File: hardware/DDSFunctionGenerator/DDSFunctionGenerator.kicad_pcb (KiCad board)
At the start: 2 copper layers, 100 x 80 mm, 126 parts, among them J1 Conn_Coaxial, J2 USB_B_Micro, J3 Conn_Coaxial, J4 Conn_Coaxial, Q1 Q_NPN_BEC, Q2 Q_NPN_BEC, Q3 Q_NPN_BEC, SW1 Rotary_Encoder_Switch, T1 Transformer_1P_1S, U1 TC1107-3.3VOA, U10 74HCT1G86, U2 L7805, U3 L7805, U4 AD9832, U5 STM32F030K6Tx, U6 FT200XD, U7 AD8325, U8 MCP3425A0T-ECH, X1 XO91, Y1 Crystal

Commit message: before trying to remove "rescue" nonsense
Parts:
- moved C24 12.5 mm to (93.1, 116.6)
- moved C25 12.5 mm to (98.4, 116.6)
- moved Y1 12.5 mm to (93.8, 119.8)
- moved R32 12.5 mm to (94.1, 124.6)
- moved R33 12.5 mm to (94.4, 128.2)
- moved U5 12.5 mm to (85.5, 127.4)
- moved C38 7.47 mm to (121.4, 120.9)
- moved J2 7.47 mm to (147.5, 128.1)
- moved R31 7.47 mm to (139.1, 130.4)
- moved U6 7.47 mm to (141.1, 125.5)
- moved C26 7.47 mm to (143.5, 130.4)
- moved C40 7.47 mm to (125.7, 110.0)
- moved D11 7.47 mm to (131.8, 95.5)
- moved D6 7.47 mm to (132.8, 120.1)
- moved D8 7.47 mm to (132.8, 112.5)
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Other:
- board size 100 x 80 mm -> 100 x 70 mm

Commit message: further routing
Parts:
- L4, L5, L6, L7, L8: footprint Inductor_THT:L_Axial_L5.3mm_D2.2mm_P7.62mm_Horizontal_Vishay_IM-1 -> Inductor_THT:L_Axial_L7.0mm_D3.3mm_P2.54mm_Vertical_Fastron_MICC
- moved C47 28.0 mm to (63.5, 72.1)
- moved C14 14.3 mm to (80.3, 97.5), turned to 180 degrees
- moved C13 10.0 mm to (79.7, 90.4), turned to 0 degrees
- moved C12 9.08 mm to (76.7, 91.4), turned to 90 degrees
- moved C19 8.22 mm to (58.4, 97.5), turned to 90 degrees
- moved R2 6.62 mm to (71.6, 83.3)
- moved R28 6.62 mm to (71.6, 81.3)
- moved R29 6.62 mm to (71.6, 85.3)
- moved C3 6.10 mm to (91.9, 117.3)
- moved C5 6.10 mm to (66.7, 108.1)
- moved C6 6.10 mm to (92.4, 107.7)
- moved C8 6.10 mm to (76.4, 107.6)
- moved C9 6.10 mm to (103.1, 108.2)
- moved L1 6.10 mm to (98.0, 108.2)
- moved L2 6.10 mm to (72.0, 107.6)
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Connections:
- net /DDSSynthesizer/MCLK renamed Net-(C47-Pad2)
- Rel1 pad 1: Net-(D1-Pad2) -> +9V
- Rel1 pad 3: Net-(Rel1-Pad3) -> RF_FROM_AMPLIFIER
- Rel1 pad 4: Net-(R6-Pad1) -> Net-(R10-Pad1)
- Rel1 pad 5: Net-(R10-Pad1) -> Net-(R6-Pad1)
- Rel1 pad 6: RF_FROM_AMPLIFIER -> Net-(Rel1-Pad6)
- Rel1 pad 8: +9V -> Net-(D1-Pad2)
- Rel2 pad 1: Net-(D2-Pad2) -> +9V
- Rel2 pad 3: Net-(Rel2-Pad3) -> Net-(Rel1-Pad6)
- Rel2 pad 4: Net-(R14-Pad1) -> Net-(R16-Pad1)
- Rel2 pad 5: Net-(R16-Pad1) -> Net-(R14-Pad1)
- Rel2 pad 6: Net-(Rel1-Pad3) -> Net-(Rel2-Pad6)
- Rel2 pad 8: +9V -> Net-(D2-Pad2)
- Rel3 pad 1: Net-(D3-Pad2) -> +9V
- Rel3 pad 3: Net-(J1-Pad1) -> Net-(Rel2-Pad6)
- Rel3 pad 4: Net-(R22-Pad1) -> Net-(R24-Pad1)
- Rel3 pad 5: Net-(R24-Pad1) -> Net-(R22-Pad1)
- Rel3 pad 6: Net-(Rel2-Pad3) -> Net-(J1-Pad1)
- Rel3 pad 8: +9V -> Net-(D3-Pad2)
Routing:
- net +9V: track 11.8 -> 2.47 mm
- net SLEEP: track 9.18 -> 0.00 mm
- net Net-(L4-Pad1): track 16.0 -> 7.02 mm
- net PSEL0: track 8.32 -> 0.00 mm
- net PSEL1: track 7.61 -> 0.00 mm
- net TXEN: track 7.29 -> 0.00 mm
- net SDATA: track 6.99 -> 0.00 mm
- net RF_DDS: track 12.6 -> 5.59 mm
- net FSELECT: track 7.48 -> 1.13 mm
- net CLK: track 4.92 -> 0.00 mm
- net SCLK: track 4.11 -> 0.00 mm
- net Net-(R16-Pad1): track 10.4 -> 6.57 mm
- net Net-(R10-Pad1): track 10.3 -> 6.53 mm
- net Net-(R6-Pad1): track 10.2 -> 6.54 mm
- net Net-(R22-Pad1): track 10.3 -> 6.67 mm
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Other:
- board size 100 x 70 mm -> 95 x 70 mm

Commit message: further routing
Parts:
- moved C12 14.6 mm to (79.8, 77.2), turned to 270 degrees
- moved L7 8.10 mm to (80.8, 81.3)
- moved C13 6.43 mm to (81.8, 84.3)
- moved C15 5.98 mm to (84.8, 86.9)
- moved C16 5.85 mm to (85.3, 89.9)
- moved L5 5.44 mm to (80.8, 73.2)
- moved C14 4.60 mm to (80.8, 93.0)
- moved R3 4.33 mm to (85.9, 81.3), turned to 90 degrees
- moved L8 3.75 mm to (80.8, 87.9), turned to 270 degrees
- moved L6 3.23 mm to (84.8, 77.2), turned to 180 degrees
- moved TP6 2.81 mm to (86.9, 93.0)
- moved C10 2.42 mm to (85.9, 69.1), turned to 90 degrees
- moved L4 1.61 mm to (80.8, 69.1), turned to 0 degrees
- moved C11 1.08 mm to (85.9, 73.2), turned to 270 degrees
- moved C1 1.02 mm to (67.4, 82.7)
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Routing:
- net Net-(C13-Pad2): track 13.1 -> 0.00 mm
- net Net-(L4-Pad1): track 7.02 -> 0.00 mm
- net Net-(C11-Pad2): track 6.22 -> 0.00 mm
- net RF_DDS: track 5.59 -> 0.00 mm

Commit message: further routing
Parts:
- added C41: 100n, Capacitor_SMD:C_0805_2012Metric_Pad1.15x1.40mm_HandSolder, F.Cu at (61.0, 72.1)
- added J5: Conn_Coaxial, Connector_Coaxial:U.FL_Molex_MCRF_73412-0110_Vertical, F.Cu at (56.4, 71.6)
- added J6: Conn_Coaxial, Connector_Coaxial:U.FL_Molex_MCRF_73412-0110_Vertical, F.Cu at (55.9, 76.7)
- added JP2: Jumper_NO_Small, Connector_PinHeader_2.54mm:PinHeader_2x01_P2.54mm_Vertical, F.Cu at (59.9, 67.1)
- added JP3: SolderJumper_2_Open, Jumper:SolderJumper-2_P1.3mm_Open_TrianglePad1.0x1.5mm, F.Cu at (67.1, 78.4)
- added R36: 0R, Resistor_SMD:R_0805_2012Metric_Pad1.15x1.40mm_HandSolder, F.Cu at (61.5, 75.2)
- added R37: 50R, Resistor_SMD:R_0805_2012Metric_Pad1.15x1.40mm_HandSolder, F.Cu at (56.4, 81.3)
- added TP1: TestPoint, TestPoint:TestPoint_Pad_1.5x1.5mm, F.Cu at (65.0, 74.7)
- moved TP4 3.70 mm to (66.8, 83.1)
- moved C1 3.70 mm to (66.3, 86.2)
- moved C4 3.70 mm to (62.2, 94.0)
- moved C7 3.70 mm to (61.9, 86.2)
- moved JP1 3.70 mm to (58.4, 86.7)
- moved X1 3.70 mm to (59.4, 84.1)
- moved U1 3.70 mm to (64.1, 90.2)
- moved J3 0.80 mm to (138.7, 115.3)
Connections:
- J2 pad 2: Net-(J2-Pad2) -> (no net)
- J2 pad 3: Net-(J2-Pad3) -> (no net)
- J2 pad 4: Net-(J2-Pad4) -> (no net)
- Q3 pad 3: Net-(Q3-Pad3) -> (no net)
- R12 pad 2: REL_2 -> (no net)
- R20 pad 2: REL_3 -> (no net)
- R32 pad 1: Net-(R32-Pad1) -> (no net)
- R32 pad 2: Net-(R32-Pad2) -> (no net)
- R33 pad 1: Net-(R33-Pad1) -> (no net)
- R33 pad 2: Net-(R33-Pad2) -> (no net)
- R4 pad 2: REL_1 -> (no net)
- U1 pad 3: Net-(U1-Pad3) -> (no net)
- U1 pad 6: Net-(U1-Pad6) -> (no net)
- U1 pad 7: Net-(U1-Pad7) -> (no net)
- U10 pad 1: DIGITAL_OUTT_1 -> (no net)
- U4 pad 6: Net-(C47-Pad2) -> /DDSSynthesizer/MCLK
- U4 pad 7: SCLK -> (no net)
- U4 pad 9: FSYNC -> (no net)
- U5 pad 1: Net-(U5-Pad1) -> (no net)
- U5 pad 10: Net-(U5-Pad10) -> (no net)
- U5 pad 11: Net-(U5-Pad11) -> (no net)
- U5 pad 12: Net-(U5-Pad12) -> (no net)
- U5 pad 13: Net-(U5-Pad13) -> (no net)
- U5 pad 14: Net-(U5-Pad14) -> (no net)
- U5 pad 15: Net-(U5-Pad15) -> (no net)
- U5 pad 16: Net-(U5-Pad16) -> (no net)
- U5 pad 17: Net-(U5-Pad17) -> (no net)
- U5 pad 18: Net-(U5-Pad18) -> (no net)
- U5 pad 19: Net-(U5-Pad19) -> (no net)
- U5 pad 2: Net-(U5-Pad2) -> (no net)
- U5 pad 20: Net-(U5-Pad20) -> (no net)
- U5 pad 21: Net-(U5-Pad21) -> (no net)
- U5 pad 22: Net-(U5-Pad22) -> (no net)
- U5 pad 23: Net-(U5-Pad23) -> (no net)
- U5 pad 24: Net-(U5-Pad24) -> (no net)
- U5 pad 25: Net-(U5-Pad25) -> (no net)
- U5 pad 26: Net-(U5-Pad26) -> (no net)
- U5 pad 27: Net-(U5-Pad27) -> (no net)
- U5 pad 28: Net-(U5-Pad28) -> (no net)
- U5 pad 29: Net-(U5-Pad29) -> (no net)
- U5 pad 3: Net-(U5-Pad3) -> (no net)
- U5 pad 30: Net-(U5-Pad30) -> (no net)
- U5 pad 31: Net-(U5-Pad31) -> (no net)
- U5 pad 32: Net-(U5-Pad32) -> (no net)
- U5 pad 4: Net-(U5-Pad4) -> (no net)
- U5 pad 5: Net-(U5-Pad5) -> (no net)
- U5 pad 6: Net-(U5-Pad6) -> (no net)
- U5 pad 7: Net-(U5-Pad7) -> (no net)
- U5 pad 8: Net-(U5-Pad8) -> (no net)
- U5 pad 9: Net-(U5-Pad9) -> (no net)
- U6 pad 1: Net-(U6-Pad1) -> (no net)
- U6 pad 10: Net-(U6-Pad10) -> (no net)
- U6 pad 11: Net-(U6-Pad11) -> (no net)
- U6 pad 2: Net-(U6-Pad2) -> (no net)
- U6 pad 3: Net-(U6-Pad3) -> (no net)
- U6 pad 4: Net-(U6-Pad4) -> (no net)
- U6 pad 5: Net-(U6-Pad5) -> (no net)
- U6 pad 6: Net-(U6-Pad6) -> (no net)
- U6 pad 7: Net-(U6-Pad7) -> (no net)
- U6 pad 8: Net-(U6-Pad8) -> (no net)
- U6 pad 9: Net-(U6-Pad9) -> (no net)
- U7 pad 1: DATAEN -> (no net)
- U7 pad 25: Net-(U7-Pad25) -> (no net)
- U7 pad 3: CLK -> (no net)
- U7 pad 6: TXEN -> (no net)
- U7 pad 7: SLEEP -> (no net)
- U8 pad 3: SCL -> (no net)
- U8 pad 4: SDA -> (no net)
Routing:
- net Net-(C47-Pad2): track 2.51 -> 0.00 mm
- net /DDSSynthesizer/MCLK: track 0.00 -> 2.51 mm

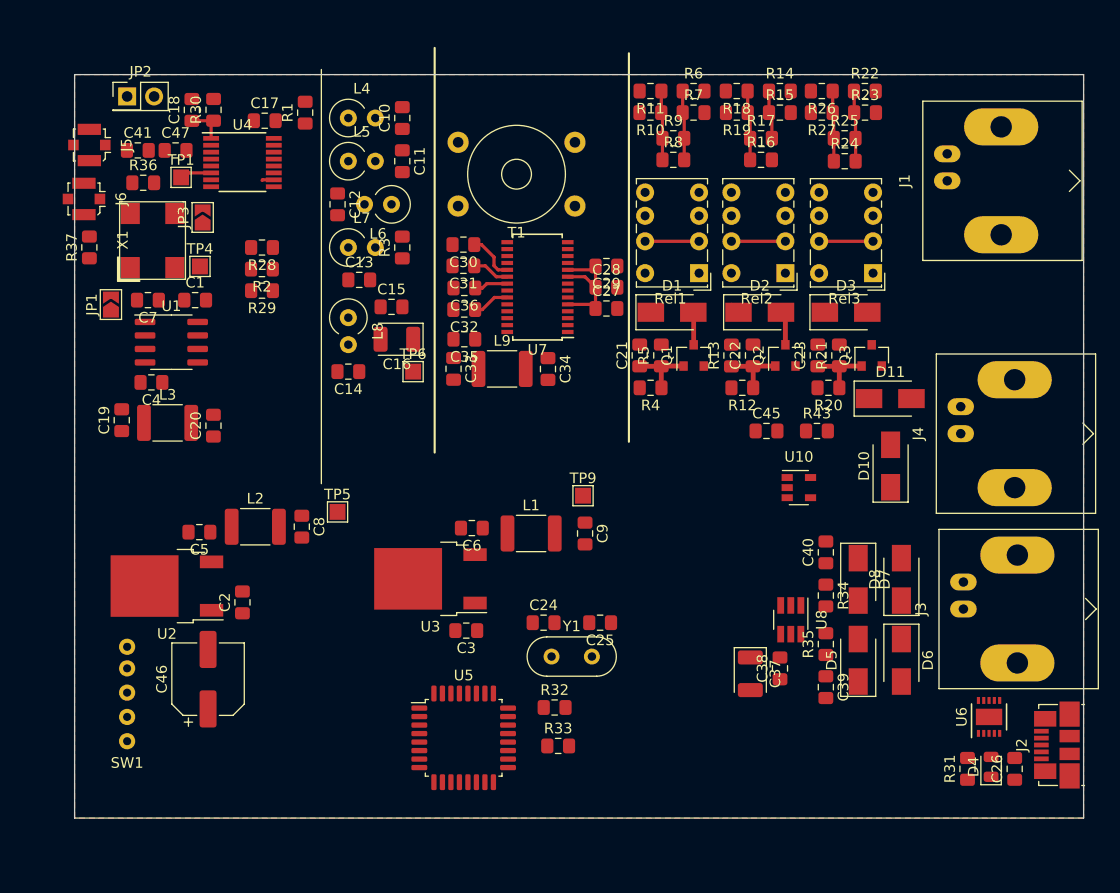
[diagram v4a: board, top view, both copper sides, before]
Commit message: model for adc/gpio socket
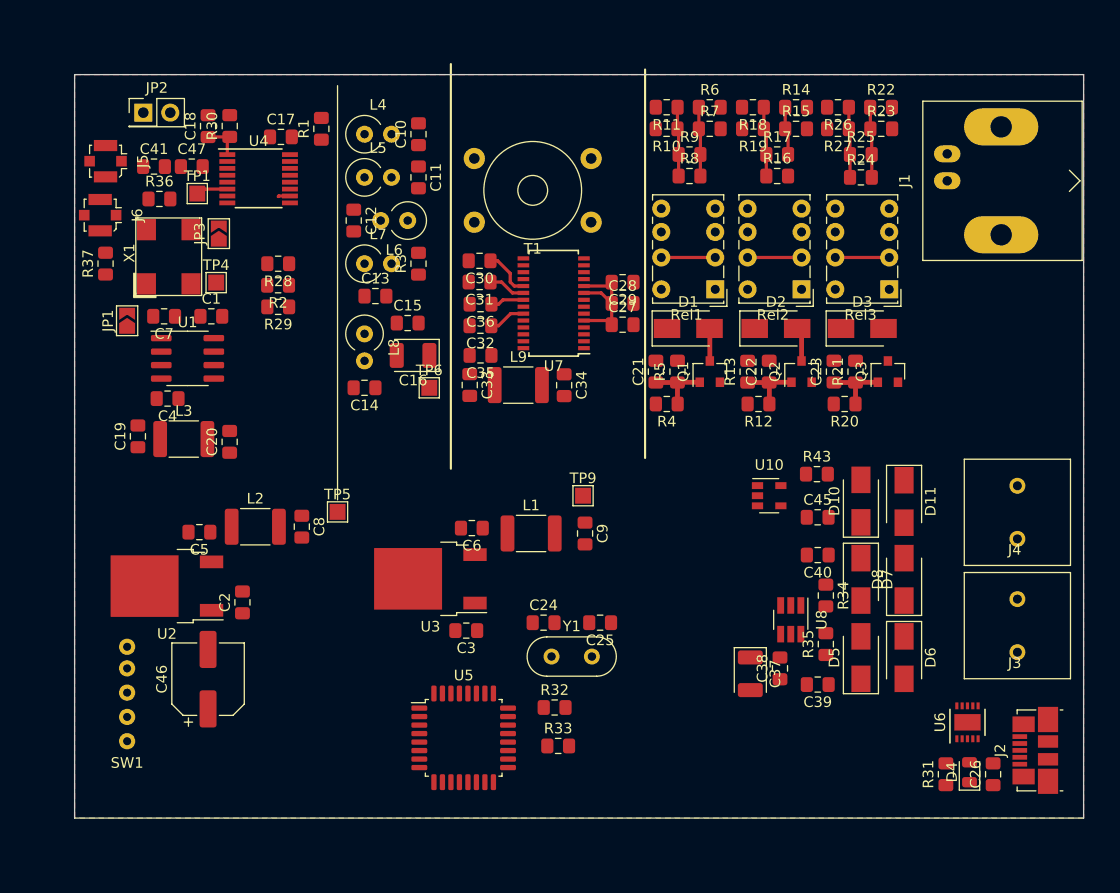
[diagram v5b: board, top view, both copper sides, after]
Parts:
- J3, J4: value Conn_Coaxial -> DG128-5.0-02P-14-00A; footprint Connector_Coaxial:BNC_Amphenol_B6252HB-NPP3G-50_Horizontal -> DDSFunctionGenerator:DG128-5.0-02P-14-00A
- X1: footprint DDSFunctionGenerator:LF SPXO018035 -> DDSFunctionGenerator:LF_SPXO018035
- moved J4 11.3 mm to (143.8, 108.7), turned to 180 degrees
- moved D11 9.77 mm to (133.1, 105.2), turned to 270 degrees
- moved C45 9.45 mm to (125.0, 106.7)
- moved J3 6.51 mm to (143.8, 119.4), turned to 180 degrees
- moved D10 4.33 mm to (129.0, 105.2)
- moved R43 4.06 mm to (124.9, 102.6)
- moved U10 2.90 mm to (120.4, 104.6)
- moved R24 2.16 mm to (129.0, 74.7)
- moved C1 2.16 mm to (67.9, 87.8)
- moved C10 2.16 mm to (87.4, 70.6)
- moved C11 2.16 mm to (87.4, 74.7)
- moved C12 2.16 mm to (81.3, 78.7)
- moved C13 2.16 mm to (83.3, 85.9)
- moved C14 2.16 mm to (82.3, 94.5)
- moved C15 2.16 mm to (86.4, 88.4)
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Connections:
- J3 pad 1: Net-(D7-Pad2) -> Net-(D5-Pad2)
- J3 pad 2: Net-(D5-Pad2) -> Net-(D7-Pad2)
- J4 pad 1: Net-(D10-Pad2) -> GND
- J4 pad 2: GND -> Net-(D10-Pad2)
- Q3 pad 3: (no net) -> Net-(D3-Pad2)

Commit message: further routing
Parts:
- removed C9: 100n, Capacitor_SMD:C_0805_2012Metric_Pad1.15x1.40mm_HandSolder
- removed L1: 4u7, Inductor_SMD:L_1812_4532Metric_Pad1.30x3.40mm_HandSolder
- removed TP5, TP9: TestPoint, TestPoint:TestPoint_Pad_1.5x1.5mm
- removed U3: L7805, Package_TO_SOT_SMD:TO-252-2
- added J7: Conn_01x04_Male, Connector_PinHeader_2.54mm:PinHeader_1x04_P2.54mm_Vertical, F.Cu at (63.5, 104.6)
- R32, R33: value 49R9 -> 2k2
- moved J2 85.3 mm to (60.5, 119.9), turned to 270 degrees
- moved C26 78.0 mm to (64.5, 118.1), turned to 270 degrees
- moved D4 73.6 mm to (66.7, 118.3), turned to 270 degrees
- moved U6 72.2 mm to (66.9, 122.4), turned to 270 degrees
- moved R31 69.2 mm to (69.0, 118.1), turned to 270 degrees
- moved C46 27.3 mm to (93.0, 112.0)
- moved C3 19.0 mm to (81.3, 101.6), turned to 270 degrees
- moved R32 17.1 mm to (113.6, 114.0)
- moved R33 17.1 mm to (113.6, 117.2)
- moved U5 16.1 mm to (103.0, 116.0), turned to 45 degrees
- moved SW1 16.0 mm to (59.0, 114.3)
- moved C24 14.2 mm to (108.2, 105.6)
- moved C25 14.2 mm to (113.5, 105.6)
- moved Y1 14.2 mm to (108.9, 108.8)
- moved C2 14.1 mm to (84.8, 112.7)
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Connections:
- C6 pad 1: Net-(C6-Pad1) -> VCC
- R12 pad 2: (no net) -> REL_2
- R20 pad 2: (no net) -> REL_3
- R4 pad 2: (no net) -> REL_1
- Rel1 pad 1: +9V -> Net-(D1-Pad2)
- Rel1 pad 3: RF_FROM_AMPLIFIER -> Net-(Rel1-Pad3)
- Rel1 pad 4: Net-(R10-Pad1) -> Net-(R6-Pad1)
- Rel1 pad 5: Net-(R6-Pad1) -> Net-(R10-Pad1)
- Rel1 pad 6: Net-(Rel1-Pad6) -> RF_FROM_AMPLIFIER
- Rel1 pad 8: Net-(D1-Pad2) -> +9V
- Rel2 pad 1: +9V -> Net-(D2-Pad2)
- Rel2 pad 3: Net-(Rel1-Pad6) -> Net-(Rel2-Pad3)
- Rel2 pad 4: Net-(R16-Pad1) -> Net-(R14-Pad1)
- Rel2 pad 5: Net-(R14-Pad1) -> Net-(R16-Pad1)
- Rel2 pad 6: Net-(Rel2-Pad6) -> Net-(Rel1-Pad3)
- Rel2 pad 8: Net-(D2-Pad2) -> +9V
- Rel3 pad 1: +9V -> Net-(D3-Pad2)
- Rel3 pad 3: Net-(Rel2-Pad6) -> Net-(J1-Pad1)
- Rel3 pad 4: Net-(R24-Pad1) -> Net-(R22-Pad1)
- Rel3 pad 5: Net-(R22-Pad1) -> Net-(R24-Pad1)
- Rel3 pad 6: Net-(J1-Pad1) -> Net-(Rel2-Pad3)
- Rel3 pad 8: Net-(D3-Pad2) -> +9V
- U4 pad 7: (no net) -> SCLK
- U4 pad 9: (no net) -> FSYNC
- U5 pad 1: (no net) -> VCC
- U5 pad 10: (no net) -> CLK
- U5 pad 11: (no net) -> TXEN
- U5 pad 12: (no net) -> SLEEP
- U5 pad 17: (no net) -> VCC
- U5 pad 20: (no net) -> PSEL1
- U5 pad 21: (no net) -> PSEL0
- U5 pad 22: (no net) -> FSELECT
- U5 pad 23: (no net) -> SDATA
- U5 pad 24: (no net) -> SCLK
- U5 pad 25: (no net) -> FSYNC
- U5 pad 28: (no net) -> REL_3
- U5 pad 29: (no net) -> REL_2
- U5 pad 30: (no net) -> REL_1
- U5 pad 5: (no net) -> VCC
- U5 pad 8: (no net) -> DATAEN
- U5 pad 9: (no net) -> SDATA
- U7 pad 1: (no net) -> DATAEN
- U7 pad 3: (no net) -> CLK
- U7 pad 6: (no net) -> TXEN
- U7 pad 7: (no net) -> SLEEP
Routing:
- net Net-(C13-Pad2): track 0.00 -> 15.1 mm
- net Net-(C12-Pad2): track 0.00 -> 9.47 mm
- net +9V: track 2.47 -> 11.8 mm
- net RF_DDS: track 0.00 -> 6.52 mm
- net Net-(C11-Pad2): track 0.00 -> 6.42 mm
- net Net-(D3-Pad2): track 0.76 -> 7.14 mm
- net Net-(C21-Pad1): track 6.17 -> 0.03 mm
- net Net-(R14-Pad1): track 4.56 -> 10.2 mm
- net Net-(L4-Pad1): track 0.00 -> 4.06 mm
- net Net-(R16-Pad1): track 6.56 -> 10.4 mm
- net Net-(R10-Pad1): track 6.51 -> 10.3 mm
- net Net-(R6-Pad1): track 6.54 -> 10.2 mm
- net Net-(R22-Pad1): track 6.64 -> 10.3 mm
- net Net-(R24-Pad1): track 6.65 -> 10.2 mm
- net Net-(D2-Pad2): track 3.82 -> 7.09 mm
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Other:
- board size 95 x 70 mm -> 95 x 60 mm
